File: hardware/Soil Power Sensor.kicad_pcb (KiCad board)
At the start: 2 copper layers, 139 x 45 mm, 76 parts, among them J1 Screw_Terminal_01x05, J2 RFShield_OnePiece, J3 UART, J4 Conn_01x03, J5 Conn_01x03_Pin, Q1 BSS123, SW1 BOOT, SW2 EN, U1 MAX9944, U10 Wio-E5 mini, U2 INA296A, U3 REF2033, U4 THS4532, U5 TPS60400DBV, U6 ADS1219, U7 74LVC1G240, U8 ESP32-C3-WROOM-02-N4, U9 FM24CL16B

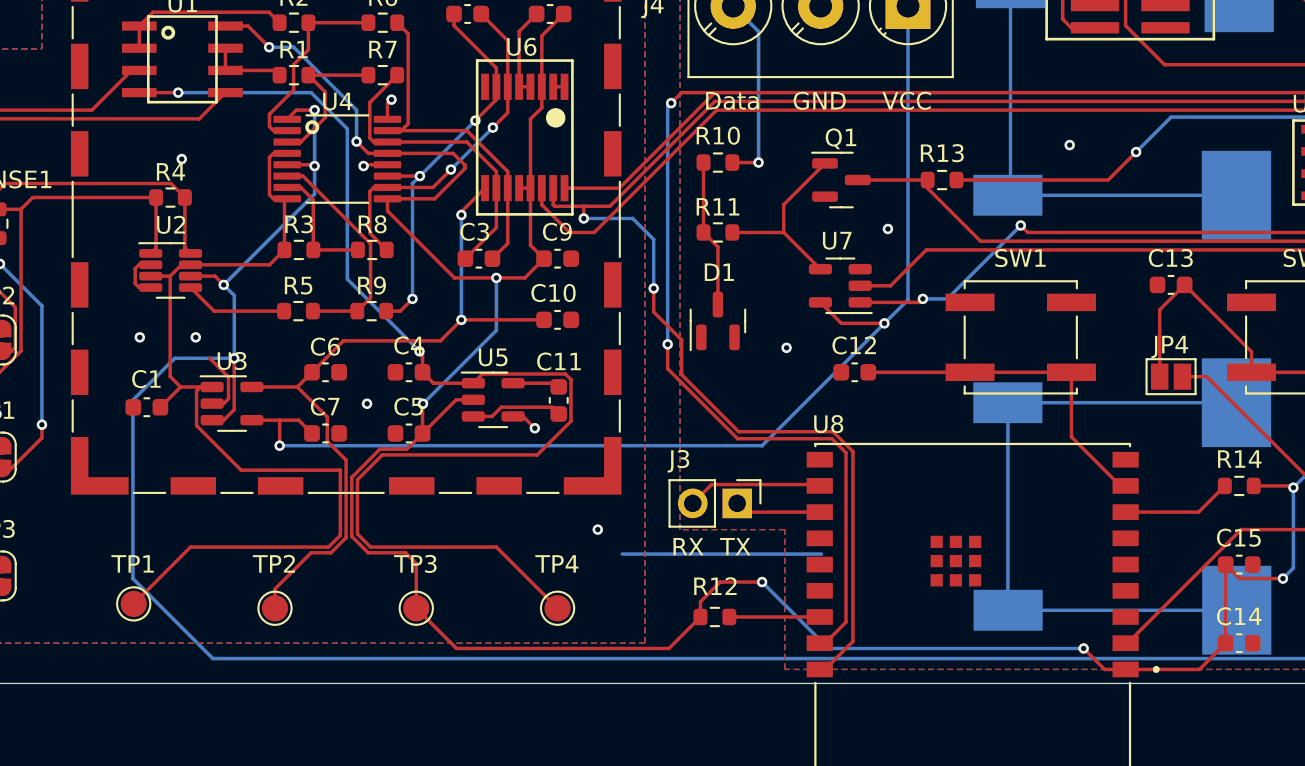
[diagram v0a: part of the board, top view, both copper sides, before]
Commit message: Updated esp32 uart terminal
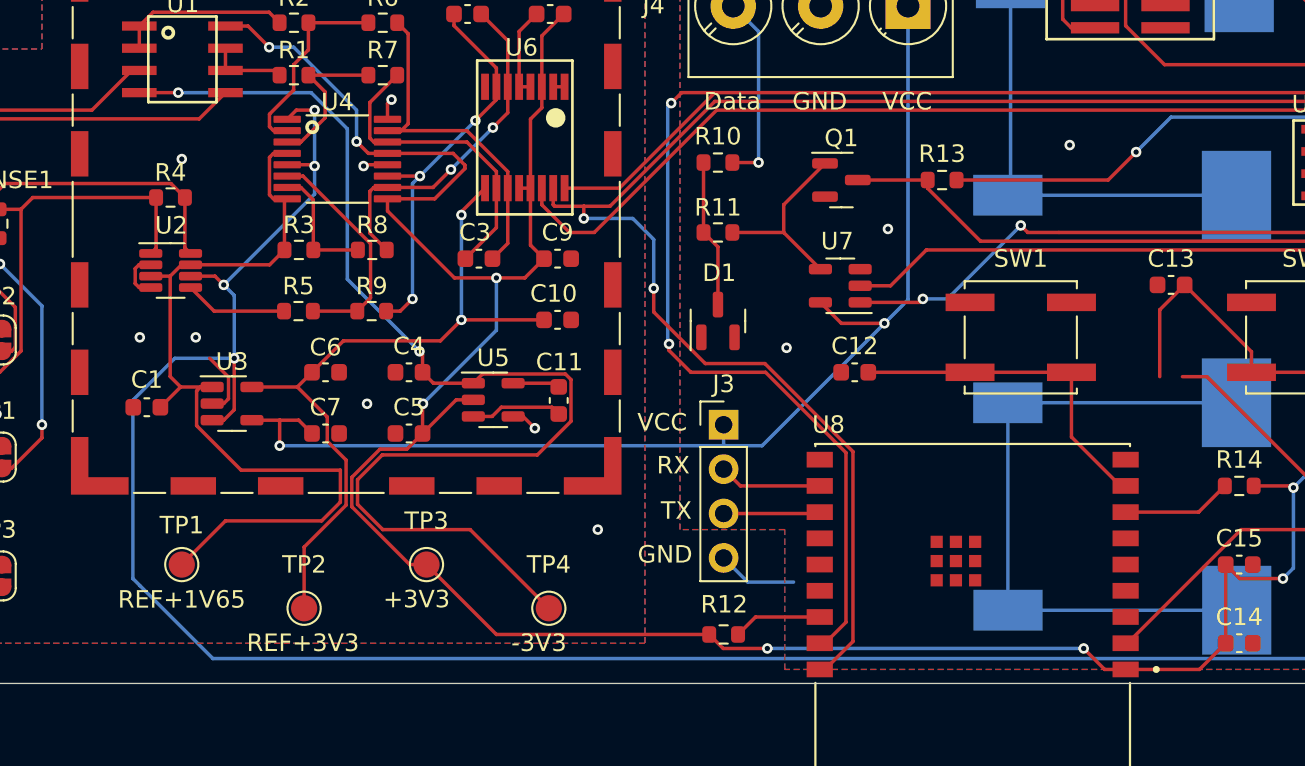
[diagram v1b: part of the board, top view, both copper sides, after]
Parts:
- removed JP4: EN_BUTTON, Jumper:SolderJumper-2_P1.3mm_Open_Pad1.0x1.5mm
- J3: footprint Connector_PinHeader_2.54mm:PinHeader_1x02_P2.54mm_Vertical -> Connector_PinHeader_2.54mm:PinHeader_1x04_P2.54mm_Vertical
- U7: value 74LVC1G240 -> SN74LVC1G240
- moved J3 4.57 mm to (170.0, 77.0), turned to 0 degrees
- moved TP1 3.55 mm to (139.0, 85.0)
- moved TP3 2.57 mm to (153.0, 85.0)
- moved TP2 1.67 mm to (146.0, 87.5)
- moved R12 1.12 mm to (170.0, 89.0)
- moved TP4 0.50 mm to (160.0, 87.5)
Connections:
- C13 pad 1: Net-(JP4-A) -> /ESP32/EN
- J3 pad 1: /ESP32/TX -> VCC
- SW2 pad 2: Net-(JP4-A) -> /ESP32/EN
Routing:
- net Net-(JP4-A): track 18.2 -> 0.00 mm
- net /ESP32/EN: track 31.2 -> 49.5 mm
- net GND: track 149.4 -> 142.6 mm
- net +3V3: track 265.7 -> 259.5 mm
- net REF+1V65: track 55.1 -> 50.3 mm
- net /ESP32/RX: track 7.74 -> 5.90 mm
- net -3V3: track 69.9 -> 68.4 mm
- net REF+3V3: track 42.6 -> 41.2 mm
- net VCC: track 178.6 -> 179.8 mm
- net /STM32/SDA: track 102.3 -> 101.2 mm
- net /STM32/SCL: track 103.5 -> 102.8 mm
- net /ESP32/TX: track 4.93 -> 5.53 mm
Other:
- board text added: "+3V3"
- board text added: "-3V3"
- board text added: "REF+1V65"
- board text added: "REF+3V3"

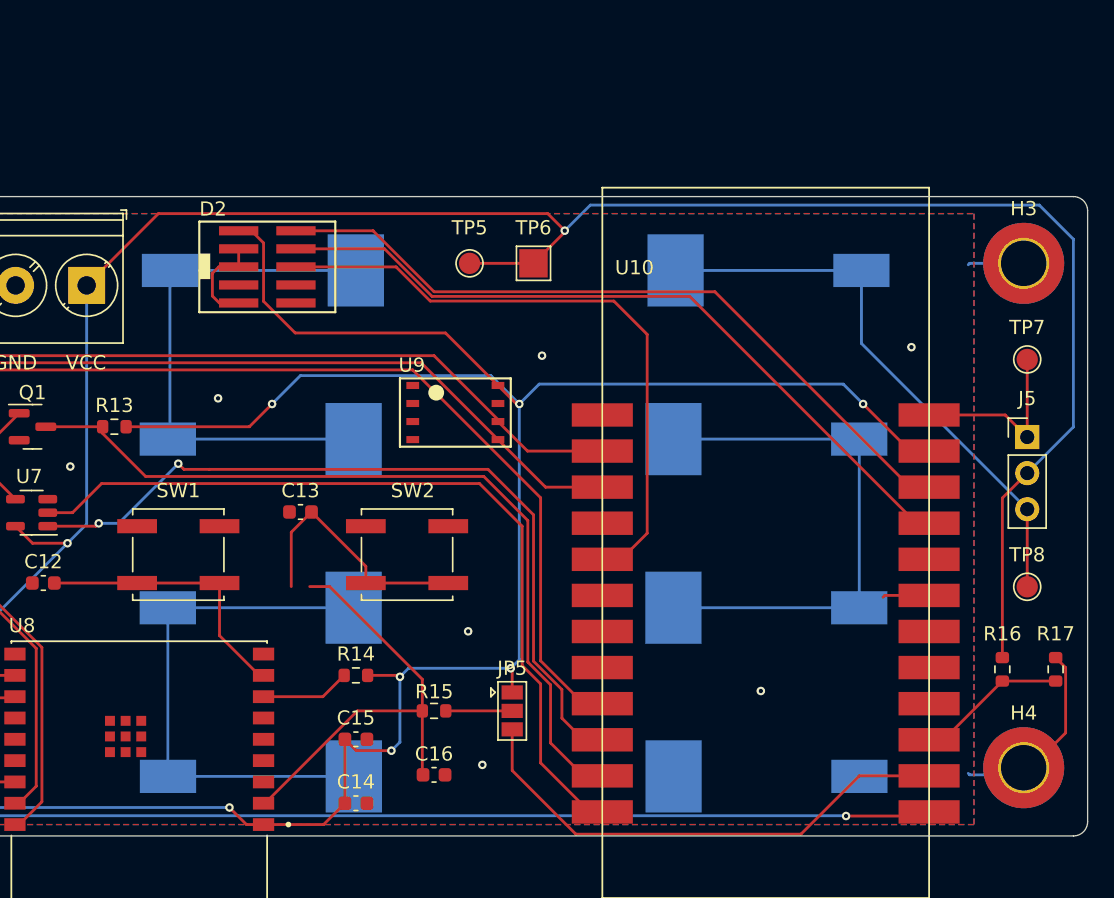
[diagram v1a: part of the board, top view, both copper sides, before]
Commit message: Added STEMMA QT connector
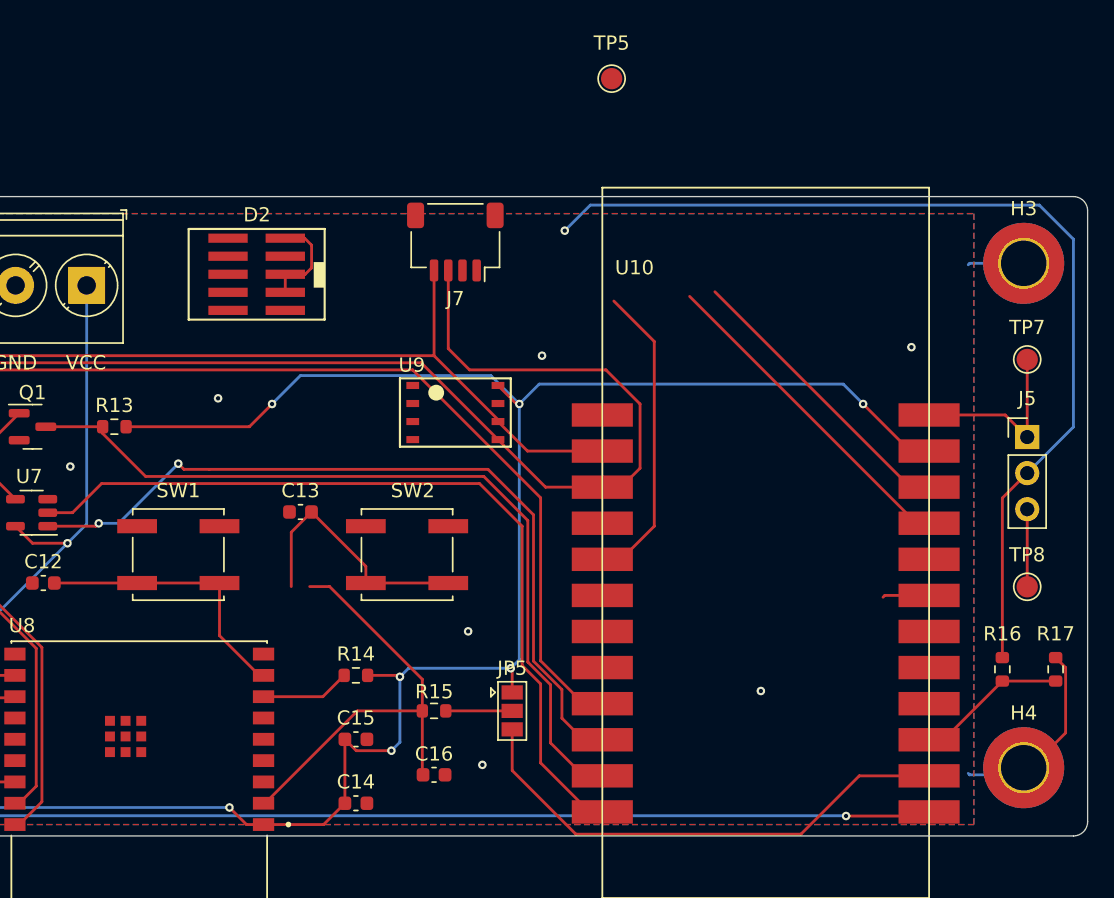
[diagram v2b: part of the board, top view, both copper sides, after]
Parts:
- removed G1, G2, G3, G4: AAA55, Soil Power Sensor:AAA55
- removed TP6: +, TestPoint:TestPoint_Pad_2.0x2.0mm
- added J7: Conn_01x04_Socket, Connector_JST:JST_SH_SM04B-SRSS-TB_1x04-1MP_P1.00mm_Horizontal, F.Cu at (206.5, 50.0)
- moved TP5 16.4 mm to (217.5, 38.5)
- moved D2 6.49 mm to (194.5, 54.8), turned to 180 degrees
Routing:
- net VCC: track 179.8 -> 135.9 mm
- net Net-(G1--): track 38.1 -> 0.00 mm
- net Net-(G3--): track 38.0 -> 0.00 mm
- net Net-(G2--): track 38.0 -> 0.00 mm
- net Net-(G1-+): track 40.2 -> 5.46 mm
- net /STM32/STM_SWDIO: track 52.0 -> 20.8 mm
- net /STM32/STM_SWDCLK: track 52.6 -> 23.5 mm
- net /STM32/SDA: track 101.2 -> 129.5 mm
- net +3V3: track 259.5 -> 234.4 mm
- net /STM32/STM_SWO: track 44.6 -> 21.6 mm
- net /STM32/SCL: track 102.8 -> 108.8 mm

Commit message: Closes #35
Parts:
- removed J5: Conn_01x03_Pin, Connector_PinHeader_2.54mm:PinHeader_1x03_P2.54mm_Vertical
- added G1: AAA55, Soil Power Sensor:AAA55, F.Cu at (178.0, -66.0)
- added G2: AAA55, Soil Power Sensor:AAA55, F.Cu at (178.0, -53.7)
- added G3: AAA55, Soil Power Sensor:AAA55, F.Cu at (178.0, -41.3)
- added G4: AAA55, Soil Power Sensor:AAA55, F.Cu at (178.0, -29.0)
- added SW3: SW_DP3T, Soil Power Sensor:JS203011JCQN, F.Cu at (248.0, 69.5)
- added TP6: +, TestPoint:TestPoint_Pad_2.0x2.0mm, F.Cu at (148.9, -20.8)
- moved TP3 100.1 mm to (148.7, -15.0)
- moved TP8 36.6 mm to (251.5, 38.0)
- moved TP5 26.5 mm to (244.0, 38.0)
- moved TP7 23.9 mm to (259.5, 38.0)
- moved D2 1.03 mm to (193.5, 54.8)
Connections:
- U10 pad 23: +3V3 -> Net-(U10-3V3)
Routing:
- net VCC: track 135.9 -> 104.4 mm
- net VUSB: track 13.0 -> 0.00 mm
- net Net-(G1-+): track 5.46 -> 0.00 mm
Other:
- board text added: "BAT"
- board text added: "USB"

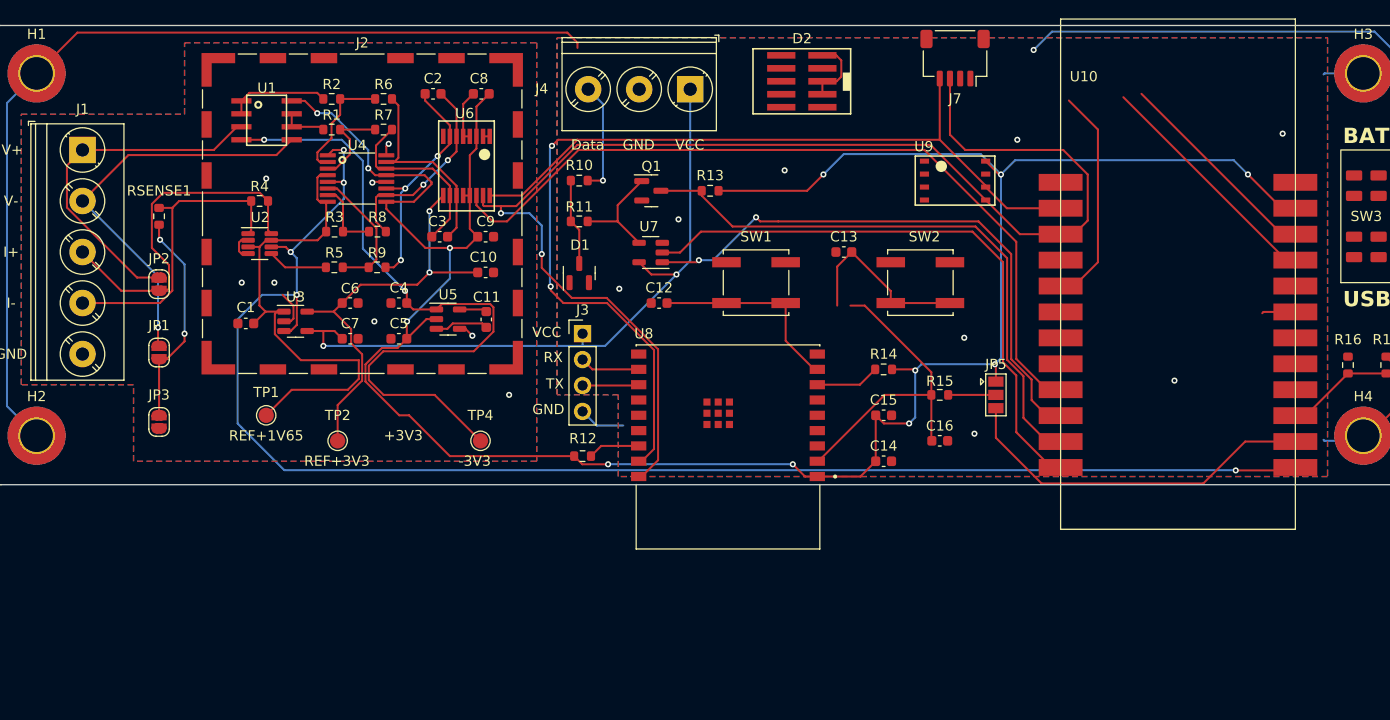
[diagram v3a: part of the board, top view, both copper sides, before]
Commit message: Closes #41
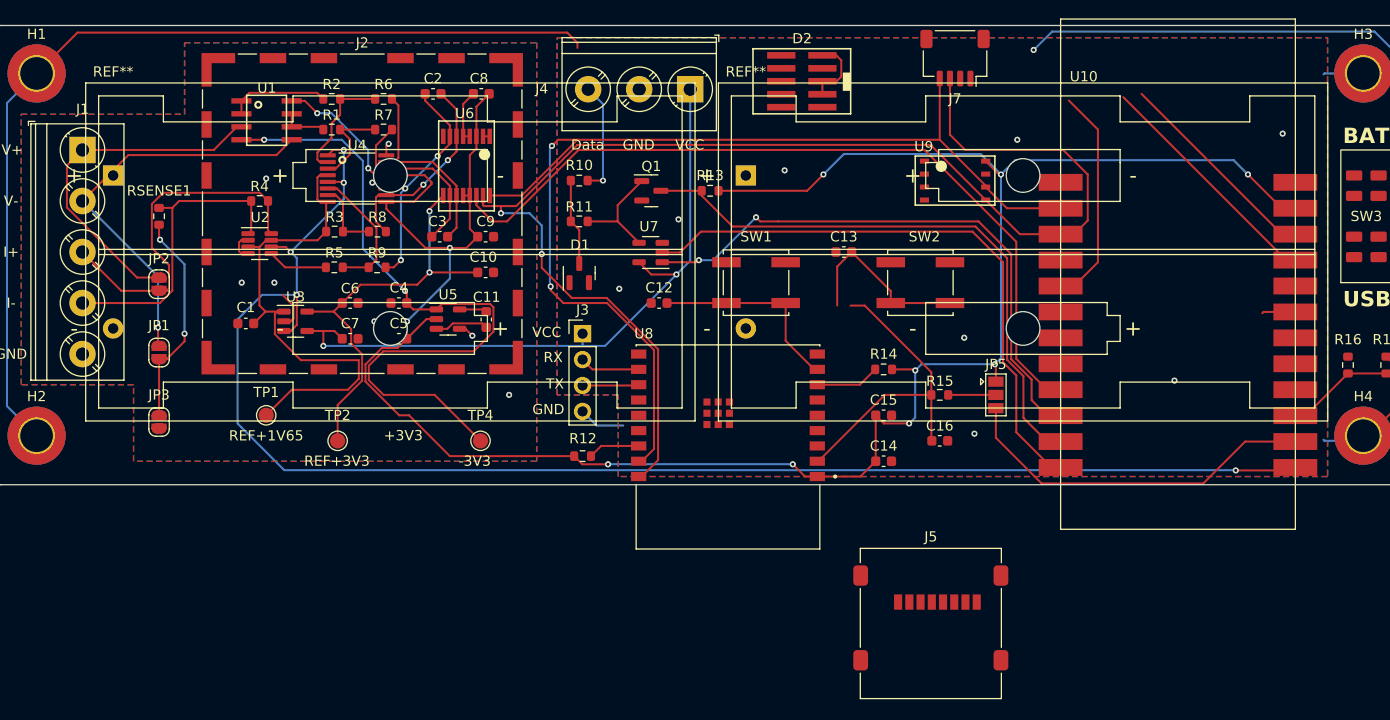
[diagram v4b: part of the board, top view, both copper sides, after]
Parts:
- added J5: Micro_SD_Card, Connector_Card:microSD_HC_Molex_47219-2001, F.Cu at (204.1, 105.4)
- added REF**: BatteryHolder_Keystone_2462_2xAA, Battery:BatteryHolder_Keystone_2462_2xAA, F.Cu at (124.0, 61.5)
- added REF**: BatteryHolder_Keystone_2462_2xAA, Battery:BatteryHolder_Keystone_2462_2xAA, F.Cu at (186.0, 61.5)
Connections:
- U8 pad 3: unconnected-(U8-IO4-Pad3) -> /ESP32/CLK
- U8 pad 4: unconnected-(U8-IO5-Pad4) -> /ESP32/SDO
- U8 pad 5: unconnected-(U8-IO6-Pad5) -> /ESP32/SDI
- U8 pad 6: unconnected-(U8-IO7-Pad6) -> /ESP32/CS

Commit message: Closes #36
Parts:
- removed G3, G4: AAA55, Soil Power Sensor:AAA55
- removed REF** (x2): BatteryHolder_Keystone_2462_2xAA, Battery:BatteryHolder_Keystone_2462_2xAA
- added JP4: SolderJumper_2_Open, Jumper:SolderJumper-2_P1.3mm_Open_RoundedPad1.0x1.5mm, F.Cu at (205.3, 30.5)
- G1: value AAA55 -> BAT1; footprint Soil Power Sensor:AAA55 -> Soil Power Sensor:Keystone2463; moved to B.Cu
- G2: value AAA55 -> BAT2; footprint Soil Power Sensor:AAA55 -> Soil Power Sensor:Keystone2463; moved to B.Cu
- moved G2 139.5 mm to (183.0, 85.8)
- moved G1 118.8 mm to (182.8, 52.8), turned to 180 degrees
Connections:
- G2 pad 2: Net-(G2--) -> GND
